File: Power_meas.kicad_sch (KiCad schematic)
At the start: 10 parts, among them U3 INA230AIRGTR

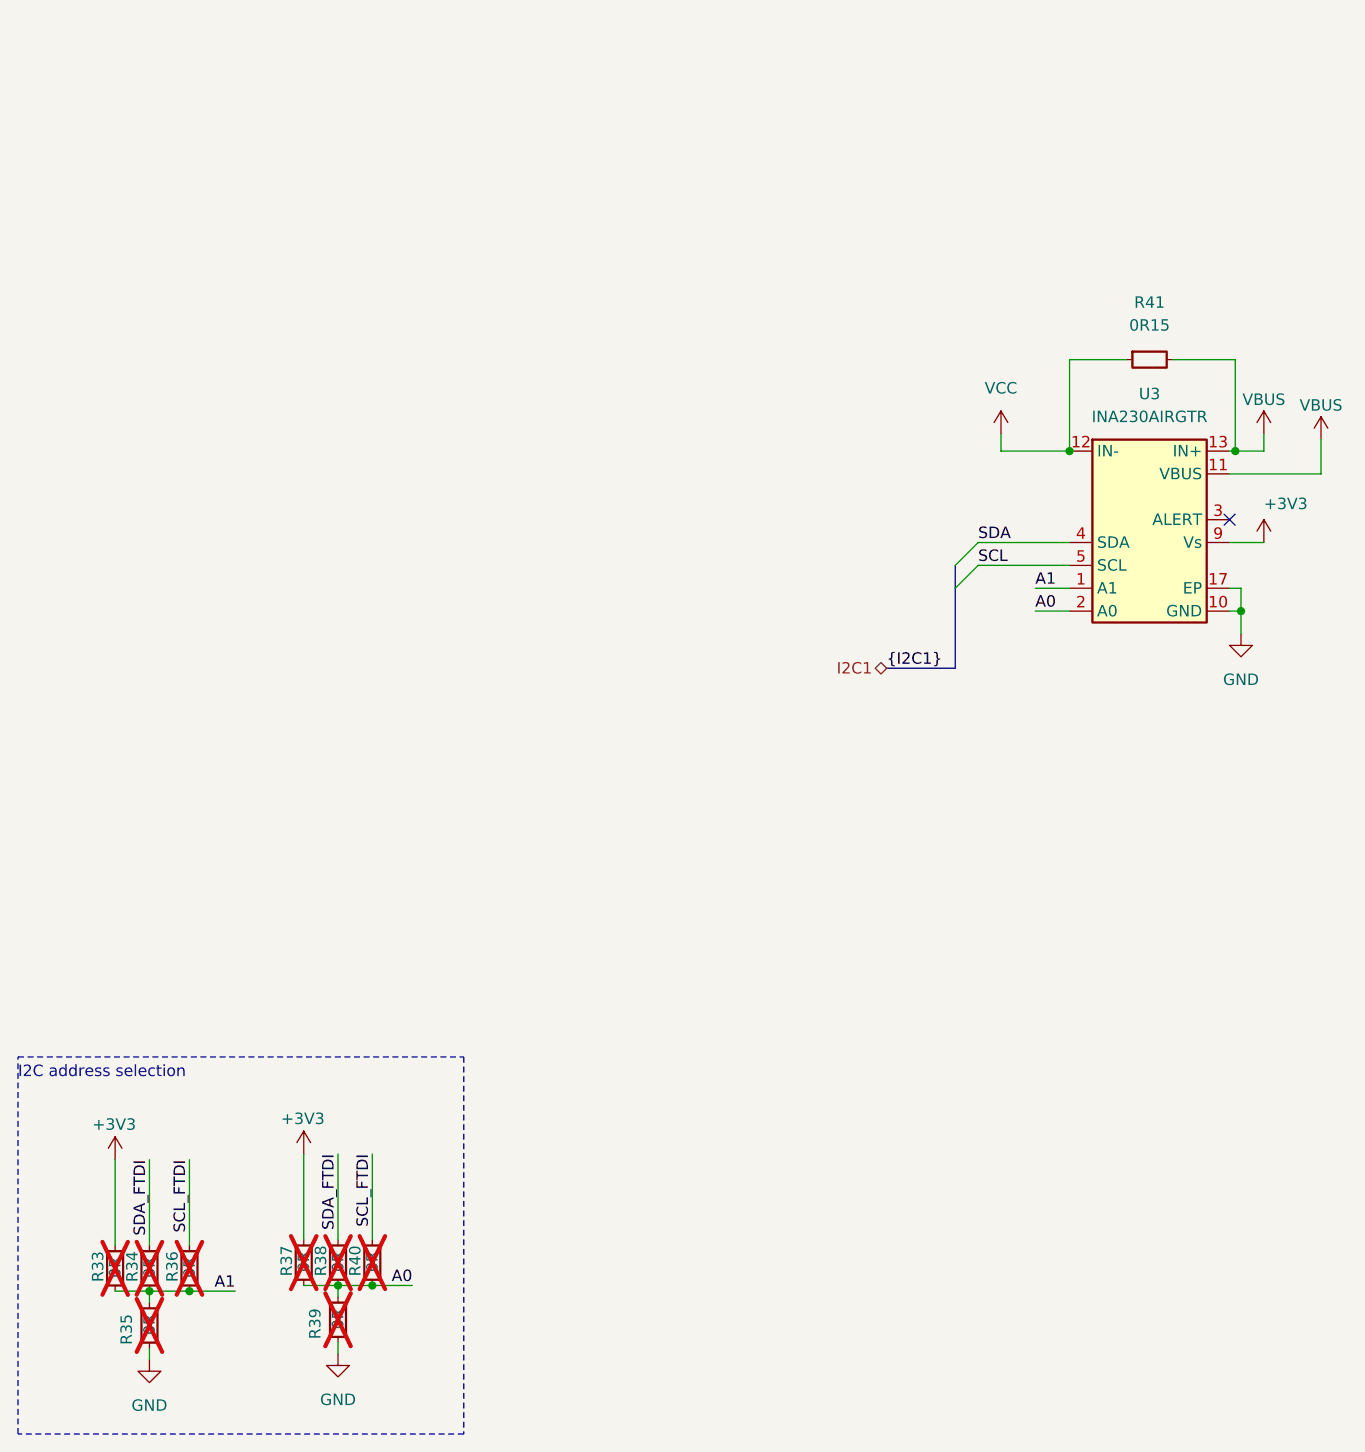
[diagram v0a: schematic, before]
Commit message: [#62623] Improve schematic, change 3V3 buck inductor, correct SPI, add testpoint
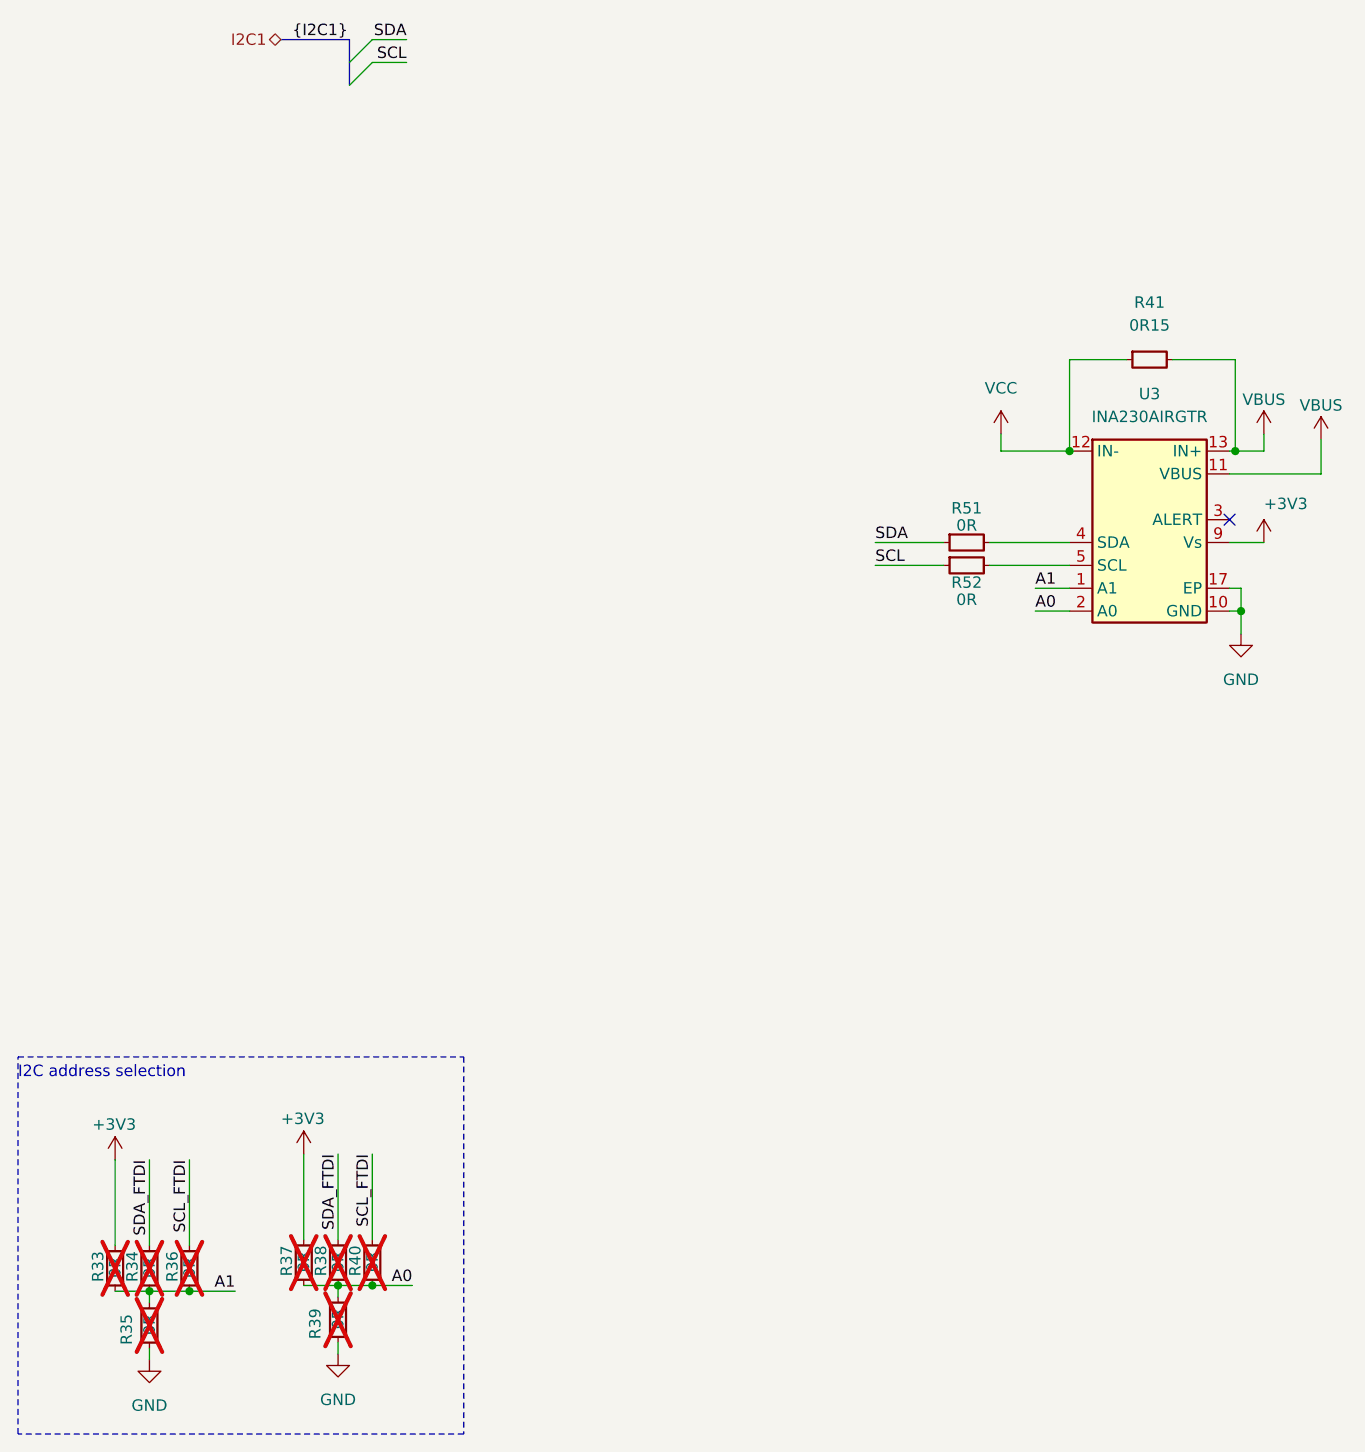
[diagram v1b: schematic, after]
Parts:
- added R51, R52: R_0R_0402, antmicro-footprints:R_0402_1005Metric, symbol antmicroResistors0402:R_0R_0402
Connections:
- net SCL: now also R52.1; no longer U3.5 (SCL)
- net SDA: now also R51.1; no longer U3.4 (SDA)
- new net: R51.2, U3.4 (SDA)
- new net: R52.2, U3.5 (SCL)
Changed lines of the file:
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@@
   )
   (no_connect (at 148.59 93.98))
-  (bus_entry (at 118.11 99.06) (size 2.54 -2.54)
-    (stroke (width 0) (type default))
-  )
-  (bus_entry (at 118.11 101.6) (size 2.54 -2.54)
+  (bus_entry (at 50.8 43.18) (size 2.54 -2.54)
+    (stroke (width 0) (type default))
+  )
+  (bus_entry (at 50.8 45.72) (size 2.54 -2.54)
     (stroke (width 0) (type default))
   )
@@
     (stroke (width 0) (type default))
   )
-  (wire (pts (xy 120.65 96.52) (xy 130.81 96.52))
-    (stroke (width 0) (type default))
-  )
-  (wire (pts (xy 120.65 99.06) (xy 130.81 99.06))
-    (stroke (width 0) (type default))
-  )
   (wire (pts (xy 24.765 179.705) (xy 28.575 179.705))
     (stroke (width 0) (type default))
@@
     (stroke (width 0) (type default))
   )
-  (bus (pts (xy 110.49 110.49) (xy 118.11 110.49))
+  (wire (pts (xy 109.22 99.06) (xy 116.84 99.06))
+    (stroke (width 0) (type default))
+  )
+  (bus (pts (xy 43.18 40.64) (xy 50.8 40.64))
     (stroke (width 0) (type default))
   )
@@
     (stroke (width 0) (type default))
   )
-  (bus (pts (xy 118.11 99.06) (xy 118.11 101.6))
+  (wire (pts (xy 53.34 40.64) (xy 57.15 40.64))
+    (stroke (width 0) (type default))
+  )
+  (bus (pts (xy 50.8 43.18) (xy 50.8 45.72))
     (stroke (width 0) (type default))
   )
@@
     (stroke (width 0) (type default))
   )
+  (wire (pts (xy 109.22 96.52) (xy 116.84 96.52))
+    (stroke (width 0) (type default))
+  )
   (wire (pts (xy 148.59 96.52) (xy 152.4 96.52))
     (stroke (width 0) (type default))
   )
-  (bus (pts (xy 118.11 101.6) (xy 118.11 110.49))
-    (stroke (width 0) (type default))
-  )
   (wire (pts (xy 148.59 101.6) (xy 149.86 101.6))
     (stroke (width 0) (type default))
@@
     (stroke (width 0) (type default))
   )
+  (wire (pts (xy 53.34 43.18) (xy 57.15 43.18))
+    (stroke (width 0) (type default))
+  )
+  (wire (pts (xy 121.92 96.52) (xy 130.81 96.52))
+    (stroke (width 0) (type default))
+  )
   (wire (pts (xy 149.225 86.36) (xy 152.4 86.36))
     (stroke (width 0) (type default))
   )
+  (bus (pts (xy 50.8 43.18) (xy 50.8 40.64))
+    (stroke (width 0) (type default))
+  )
   (wire (pts (xy 127 101.6) (xy 130.81 101.6))
     (stroke (width 0) (type default))
@@
   )
   (wire (pts (xy 28.575 179.705) (xy 33.02 179.705))
+    (stroke (width 0) (type default))
+  )
+  (wire (pts (xy 121.92 99.06) (xy 130.81 99.06))
     (stroke (width 0) (type default))
   )
@@
     (effects (font (size 1.27 1.27)) (justify left bottom))
   )
+  (label "SDA" (at 109.22 96.52 0) (fields_autoplaced)
+    (effects (font (size 1.27 1.27)) (justify left bottom))
+  )
   (label "SDA_FTDI" (at 28.575 165.1 270) (fields_autoplaced)
     (effects (font (size 1.27 1.27)) (justify right bottom))
@@
     (effects (font (size 1.27 1.27)) (justify right bottom))
   )
-  (label "{I2C1}" (at 110.49 110.49 0) (fields_autoplaced)
+  (label "{I2C1}" (at 44.45 40.64 0) (fields_autoplaced)
     (effects (font (size 1.27 1.27)) (justify left bottom))
   )
@@
     (effects (font (size 1.27 1.27)) (justify left bottom))
   )
-  (label "SDA" (at 120.65 96.52 0)
+  (label "SDA" (at 57.15 40.64 180)
+    (effects (font (size 1.27 1.27)) (justify right bottom))
+  )
+  (label "SCL" (at 109.22 99.06 0) (fields_autoplaced)
     (effects (font (size 1.27 1.27)) (justify left bottom))
   )
-  (label "SCL" (at 120.65 99.06 0)
-    (effects (font (size 1.27 1.27)) (justify left bottom))
-  )
-  (hierarchical_label "I2C1" (shape bidirectional) (at 110.49 110.49 180) (fields_autoplaced)
+  (label "SCL" (at 57.15 43.18 180)
+    (effects (font (size 1.27 1.27)) (justify right bottom))
+  )
+  (hierarchical_label "I2C1" (shape bidirectional) (at 43.18 40.64 180) (fields_autoplaced)
     (effects (font (size 1.27 1.27)) (justify right))
   )
@@
     )
   )
+  (symbol (lib_id "antmicroResistors0402:R_0R_0402") (at 116.84 99.06 0) (unit 1)
+    (in_bom yes) (on_board yes) (dnp no)
+    (property "Reference" "R52" (at 119.38 100.965 0)
+      (effects (font (size 1.27 1.27) (thickness 0.15)))
+    )
+    (property "Value" "R_0R_0402" (at 137.16 111.76 0)
+      (effects (font (size 1.27 1.27) (thickness 0.15)) (justify left bottom) hide)
+    )
+    (property "Footprint" "antmicro-footprints:R_0402_1005Metric" (at 137.16 114.3 0)
+      (effects (font (size 1.27 1.27) (thickness 0.15)) (justify left bottom) hide)
+    )
+    (property "Datasheet" "https://industrial.panasonic.com/cdbs/www-data/pdf/RDA0000/AOA0000C301.pdf" (at 137.16 116.84 0)
+      (effects (font (size 1.27 1.27) (thickness 0.15)) (justify left bottom) hide)
+    )
+    (property "MPN" "ERJ2GE0R00X" (at 137.16 119.38 0)
+      (effects (font (size 1.27 1.27) (thickness 0.15)) (justify left bottom) hide)
+    )
+    (property "Manufacturer" "Panasonic" (at 137.16 121.92 0)
+      (effects (font (size 1.27 1.27) (thickness 0.15)) (justify left bottom) hide)
+    )
+    (property "License" "Apache-2.0" (at 137.16 124.46 0)
+      (effects (font (size 1.27 1.27) (thickness 0.15)) (justify left bottom) hide)
+    )
+    (property "Author" "Antmicro" (at 137.16 127 0)
+      (effects (font (size 1.27 1.27) (thickness 0.15)) (justify left bottom) hide)
+    )
+    (property "Val" "0R" (at 119.38 102.87 0)
+      (effects (font (size 1.27 1.27) (thickness 0.15)))
+    )
+    (property "Tolerance" "~" (at 137.16 109.22 0)
+      (effects (font (size 1.27 1.27)) (justify left bottom) hide)
+    )
+    (property "Current" "1A" (at 137.16 129.54 0)
+      (effects (font (size 1.27 1.27) (thickness 0.15)) (justify left bottom) hide)
+    )
+    (pin "2")
+    (pin "1")
+    (instances
+      (project "antmicro-poe-to-usbc-pd-adapter"
+        (path "/cf0d4429-3f03-449f-96a7-26d69371a46d/db251e01-6eeb-47fe-93bb-dcdf47418c03"
+          (reference "R52") (unit 1)
+        )
+      )
+    )
+  )
   (symbol (lib_id "antmicropower:GND") (at 28.575 187.325 0) (unit 1)
     (in_bom yes) (on_board yes) (dnp no) (fields_autoplaced)
@@
         )
       )
+    )
+  )
+  (symbol (lib_id "antmicroResistors0402:R_0R_0402") (at 116.84 96.52 0) (unit 1)
+    (in_bom yes) (on_board yes) (dnp no)
+    (property "Reference" "R51" (at 119.38 92.71 0)
+      (effects (font (size 1.27 1.27) (thickness 0.15)))
+    )
+    (property "Value" "R_0R_0402" (at 137.16 109.22 0)
+      (effects (font (size 1.27 1.27) (thickness 0.15)) (justify left bottom) hide)
+    )
+    (property "Footprint" "antmicro-footprints:R_0402_1005Metric" (at 137.16 111.76 0)
+      (effects (font (size 1.27 1.27) (thickness 0.15)) (justify left bottom) hide)
+    )
+    (property "Datasheet" "https://industrial.panasonic.com/cdbs/www-data/pdf/RDA0000/AOA0000C301.pdf" (at 137.16 114.3 0)
+      (effects (font (size 1.27 1.27) (thickness 0.15)) (justify left bottom) hide)
+    )
+    (property "MPN" "ERJ2GE0R00X" (at 137.16 116.84 0)
+      (effects (font (size 1.27 1.27) (thickness 0.15)) (justify left bottom) hide)
+    )
+    (property "Manufacturer" "Panasonic" (at 137.16 119.38 0)
+      (effects (font (size 1.27 1.27) (thickness 0.15)) (justify left bottom) hide)
+    )
+    (property "License" "Apache-2.0" (at 137.16 121.92 0)
+      (effects (font (size 1.27 1.27) (thickness 0.15)) (justify left bottom) hide)
+    )
+    (property "Author" "Antmicro" (at 137.16 124.46 0)
+      (effects (font (size 1.27 1.27) (thickness 0.15)) (justify left bottom) hide)
+    )
+    (property "Val" "0R" (at 119.38 94.615 0)
+      (effects (font (size 1.27 1.27) (thickness 0.15)))
+    )
+    (property "Tolerance" "~" (at 137.16 106.68 0)
+      (effects (font (size 1.27 1.27)) (justify left bottom) hide)
+    )
+    (property "Current" "1A" (at 137.16 127 0)
+      (effects (font (size 1.27 1.27) (thickness 0.15)) (justify left bottom) hide)
+    )
+    (pin "2")
+    (pin "1")
+    (instances
+      (project "antmicro-poe-to-usbc-pd-adapter"
+        (path "/cf0d4429-3f03-449f-96a7-26d69371a46d/db251e01-6eeb-47fe-93bb-dcdf47418c03"
+          (reference "R51") (unit 1)
+        )
+      )

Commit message: [#62623] Change hierarchy implementation
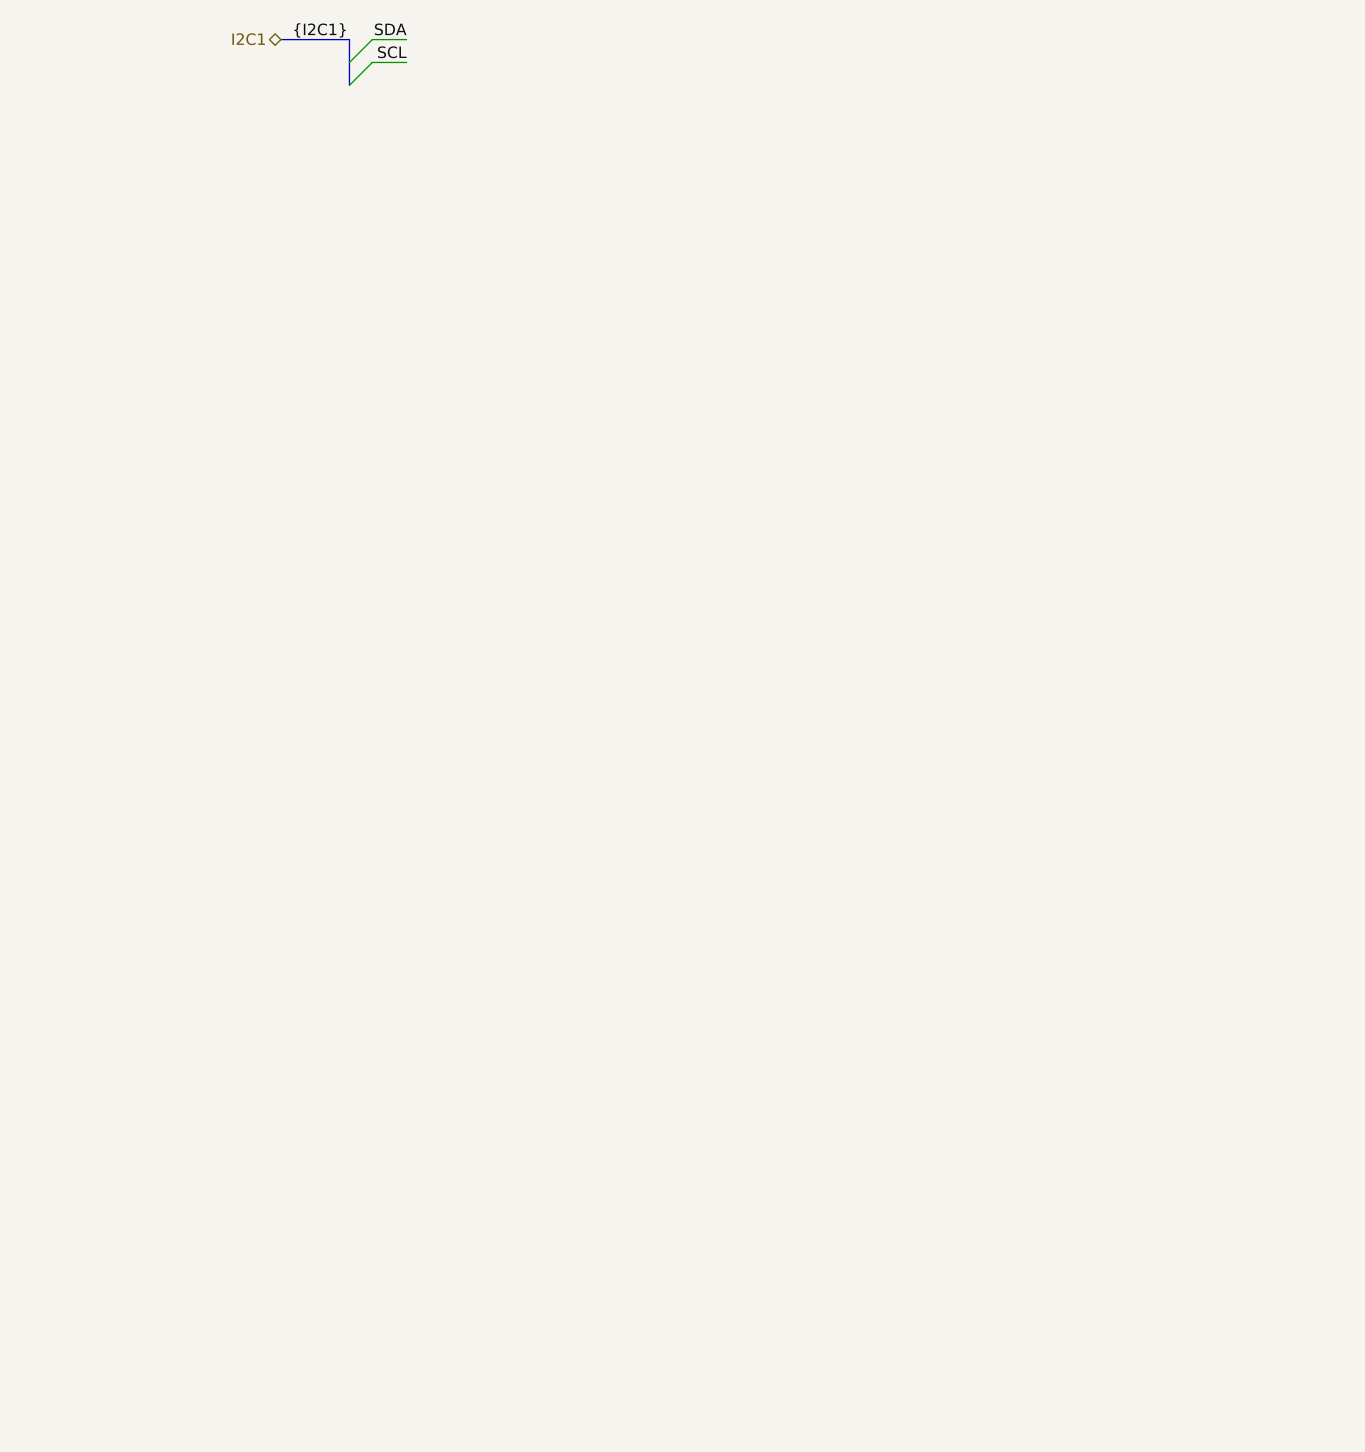
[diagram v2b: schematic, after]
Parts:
- removed R33, R34, R35, R36, R37, R38, R39, R40, R51, R52: R_0R_0402, antmicro-footprints:R_0402_1005Metric, symbol antmicroResistors0402:R_0R_0402
- removed R41: R_0R15_2010, antmicro-footprints:R_2010_5025Metric, symbol antmicroResistorsmisc:R_0R15_2010
- removed U3: INA230AIRGTR, antmicro-footprints:VQFN-16-1EP_3x3mm_P0.5mm_EP1.68x1.68mm, symbol antmicroPowerMeasurement:INA230AIRGTR
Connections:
- no-connect marks 1 -> 0
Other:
- note removed: "I2C address selection"
